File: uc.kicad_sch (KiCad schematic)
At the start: 13 parts

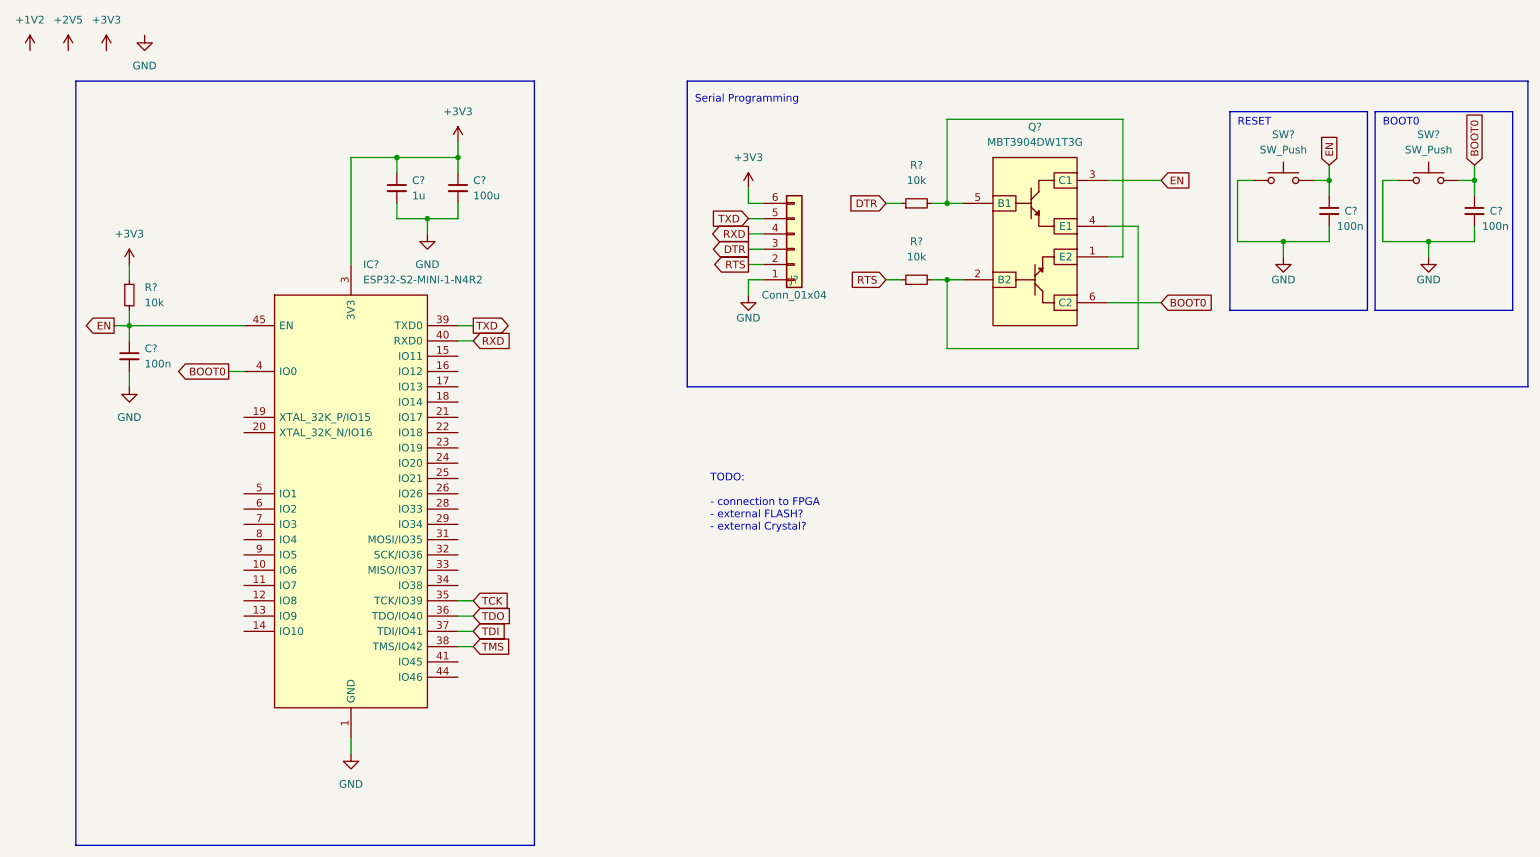
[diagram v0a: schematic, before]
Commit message: spi ESP32 implementation in uC.kicad_sch
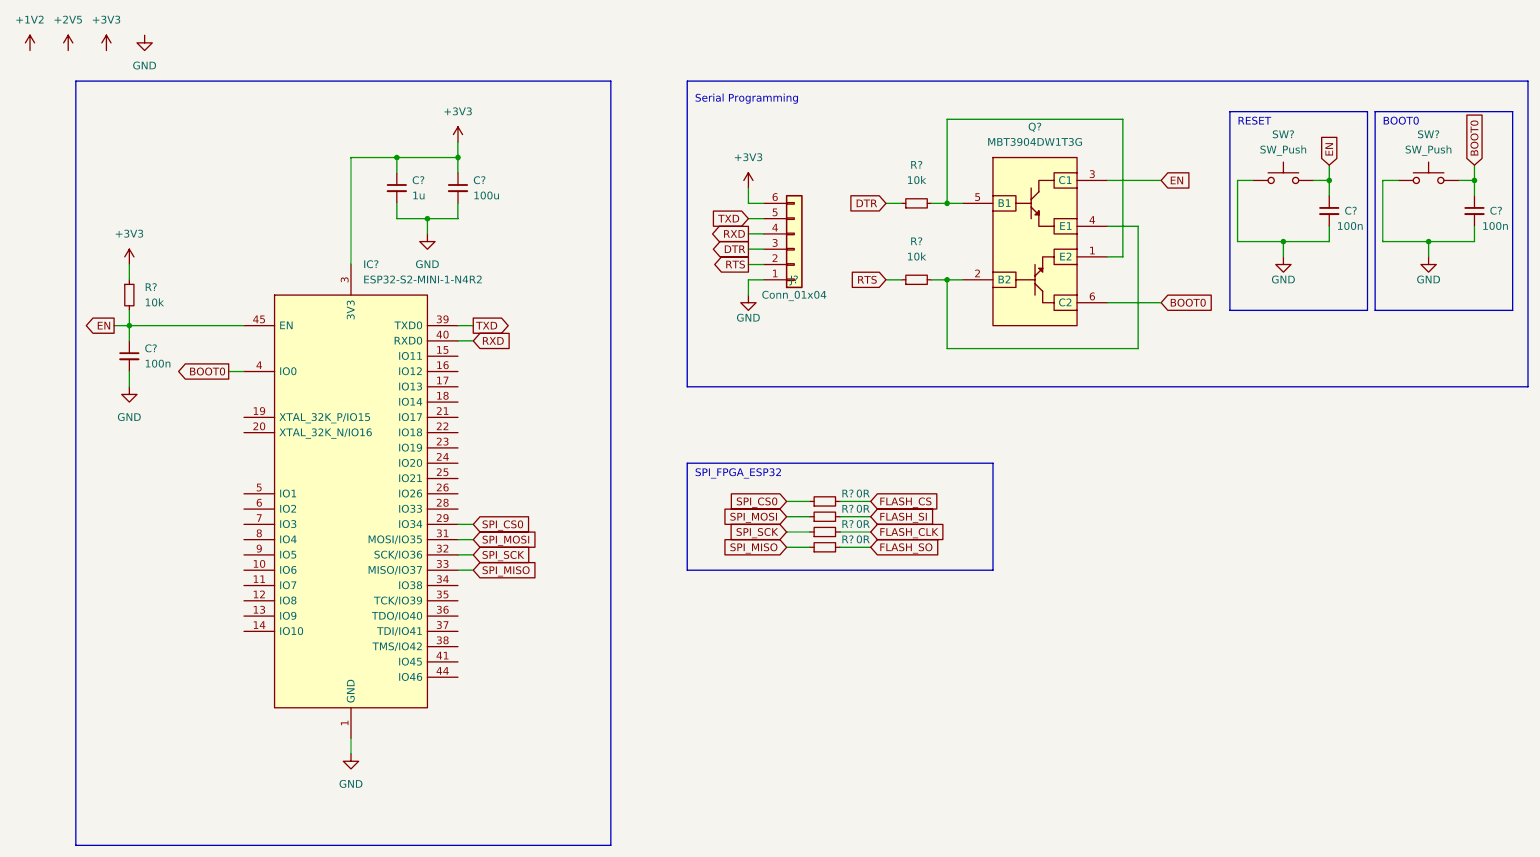
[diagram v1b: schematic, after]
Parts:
- added R? (x4): 0R, Resistor_SMD:R_0603_1608Metric_Pad0.98x0.95mm_HandSolder, symbol Device:R_Small
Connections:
- net SPI_CS0: now reaches IC?.29 (IO34)
- net SPI_CS0: now also R?.1
- net SPI_MOSI: now reaches IC?.31 (MOSI/IO35)
- net SPI_MOSI: now also R?.1
- net SPI_SCK: now reaches IC?.32 (SCK/IO36)
- net SPI_SCK: now also R?.1
- net SPI_MISO: now reaches IC?.33 (MISO/IO37)
- net SPI_MISO: now also R?.1
- net TCK: no longer names the net of IC?.35 (TCK/IO39)
- net TDI: no longer names the net of IC?.37 (TDI/IO41)
- net TDO: no longer names the net of IC?.36 (TDO/IO40)
- net TMS: no longer names the net of IC?.38 (TMS/IO42)
- new net FLASH_CLK: R?.2
- new net FLASH_CS: R?.2
- new net FLASH_SI: R?.2
- new net FLASH_SO: R?.2
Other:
- note added: "SPI_FPGA_ESP32"
- note removed: "TODO: - connection to FPGA - external FLASH? - external Crystal?"

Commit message: assigned some missing footprints
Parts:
- removed C? (x3): 100n, symbol Device:C_Small
- added C12, C15, C16: 100n/25V, Capacitor_SMD:C_0603_1608Metric_Pad1.08x0.95mm_HandSolder, symbol Device:C_Small
- C13: renamed from C?; footprint (none) -> Capacitor_SMD:C_0603_1608Metric_Pad1.08x0.95mm_HandSolder; MNR (none) -> 187-CL10A105KP8NNWC
- C14: renamed from C?; footprint (none) -> Capacitor_SMD:C_0603_1608Metric_Pad1.08x0.95mm_HandSolder; MNR (none) -> 581-F980G107MMAAH1
- J3: renamed from J?; footprint (none) -> Connector_PinHeader_2.54mm:PinHeader_1x04_P2.54mm_Vertical
- Q2: renamed from Q?; footprint SOT65P210X110-6N -> uc:SOT65P210X110-6N
- R14, R19, R20: renamed from R?; footprint (none) -> Resistor_SMD:R_0603_1608Metric_Pad0.98x0.95mm_HandSolder
- gave numbers to parts that had none: 7
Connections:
- net BOOT0: now also C16.1
- net EN: now also C12.1, C15.1
- net GND: now also C12.2, C15.2, C16.2
